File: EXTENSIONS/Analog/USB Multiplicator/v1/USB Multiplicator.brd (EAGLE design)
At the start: 30 x 63 mm, 9 parts, among them X1 USB-A

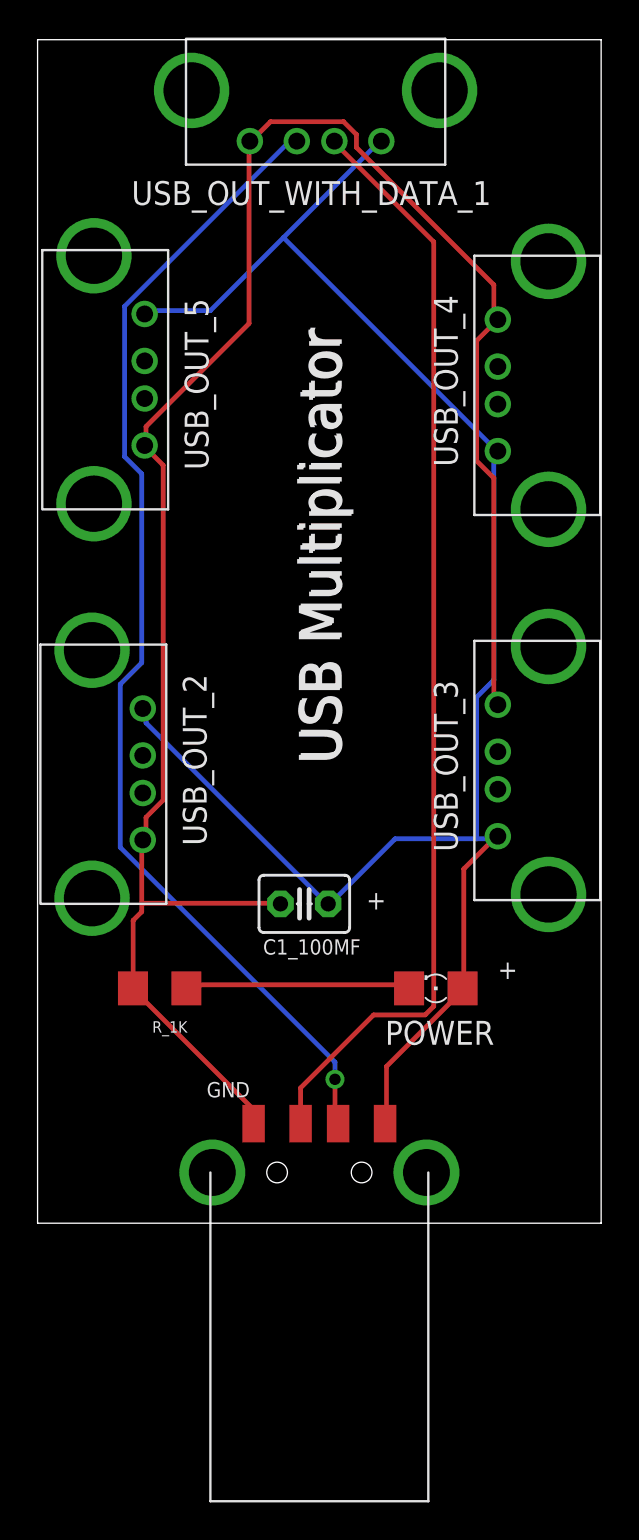
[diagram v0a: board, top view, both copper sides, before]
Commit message: Created 4017-7Segment v2
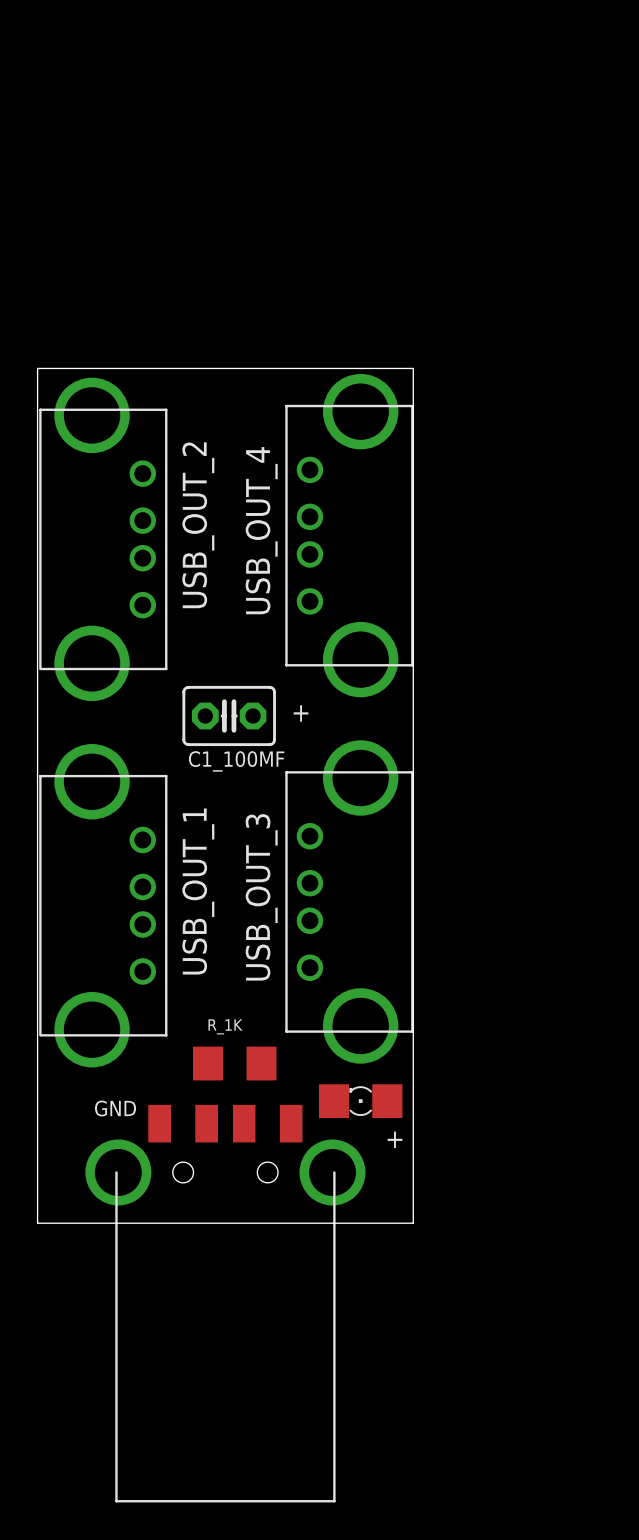
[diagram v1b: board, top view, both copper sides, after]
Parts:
- removed USB_OUT_5, USB_OUT_WITH_DATA_1: USB, STUNTAZ:USB-FEMALE-A-PTH
- added USB_OUT_1: USB, STUNTAZ:USB-FEMALE-A-PTH
- moved USB_OUT_4 12.8 mm to (15.2, 55.5)
- moved USB_OUT_2 12.5 mm to (8.90, 41.5)
- moved USB_OUT_3 12.2 mm to (15.2, 36.0)
- moved C1_100MF 10.8 mm to (12.2, 39.0)
- moved LED_PWR 7.21 mm to (19.2, 18.5)
- moved R_1K 5.66 mm to (12.5, 20.5), turned to 180 degrees
- moved X1 5.00 mm to (12.0, 14.7)
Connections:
- net GND: now also USB_OUT_1.GND; no longer USB_OUT_5.GND, USB_OUT_WITH_DATA_1.GND
- net USB_DMINUS: now also USB_OUT_1.D+; no longer USB_OUT_WITH_DATA_1.D+
- net USB_DPLUS: now also USB_OUT_1.D-; no longer USB_OUT_WITH_DATA_1.D-
- net VCC: now also USB_OUT_1.VBUS; no longer USB_OUT_5.VBUS, USB_OUT_WITH_DATA_1.VBUS
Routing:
- net GND: track 106.6 -> 0.00 mm
- net VCC: track 96.6 -> 0.00 mm
- net USB_DMINUS: track 62.1 -> 0.00 mm, vias 1 -> 0
- net USB_DPLUS: track 59.0 -> 0.00 mm
- net N$5: track 12.1 -> 0.00 mm
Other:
- board size 30 x 63 mm -> 20 x 45.5 mm
- board text added: "PCBv1 - 2017.05"
- board text removed: "PCBv2 - 2019.08"
- board text removed: "POWER"
- board text removed: "USB Multiplicator"
